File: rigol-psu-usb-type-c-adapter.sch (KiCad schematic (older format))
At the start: 12 parts

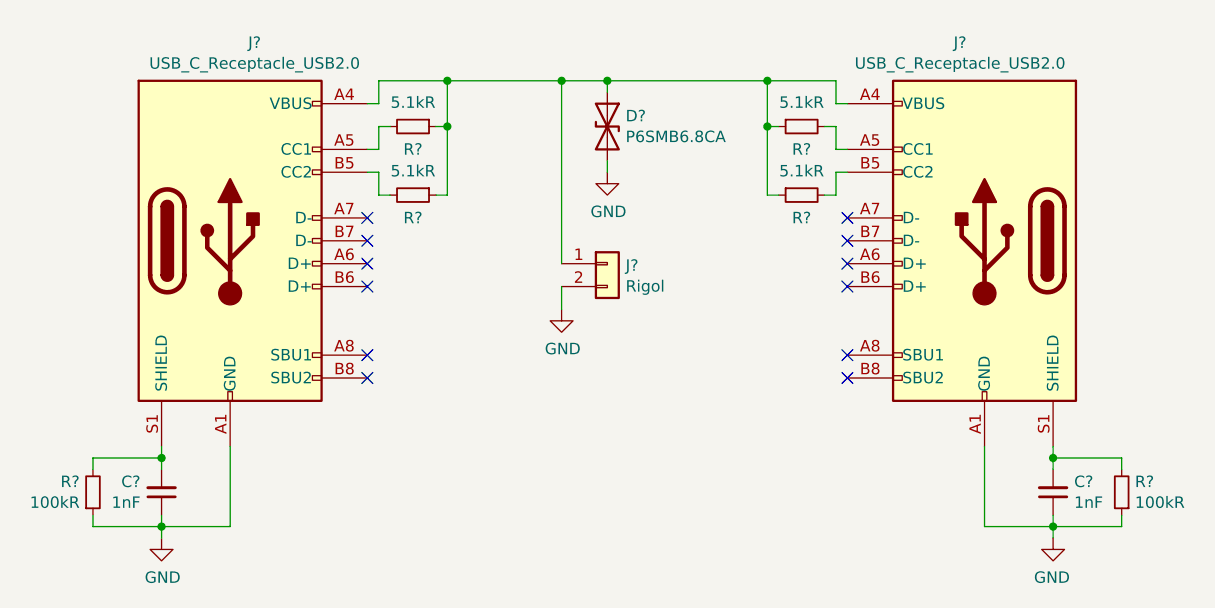
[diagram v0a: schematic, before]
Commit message: Fix CC pull-ups
Memory fooled me. They need to be 10kR, not 5.1kR.
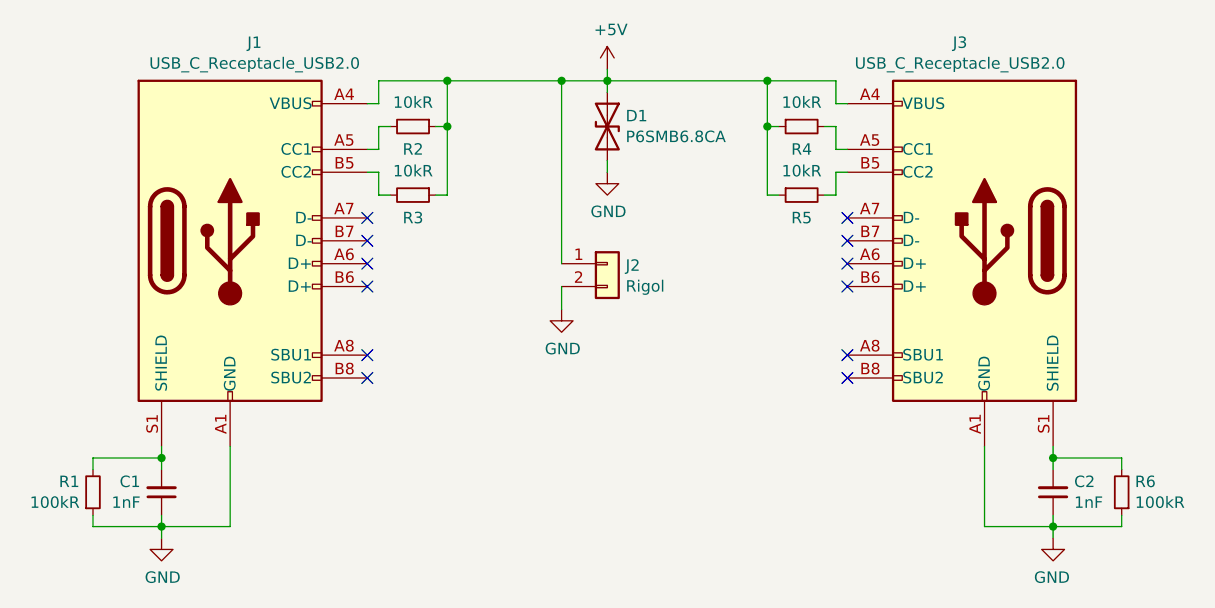
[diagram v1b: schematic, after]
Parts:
- R2, R3, R4, R5: renamed from R?; value 5.1kR -> 10kR; LCSC C25905 -> C25725
- gave numbers to parts that had none: 8
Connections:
- net +5V: now reaches D1.1 (A1), J1.A4 (VBUS), J1.A9 (VBUS), J1.B4 (VBUS), J1.B9 (VBUS), J2.1 (Pin_1), J3.A4 (VBUS), J3.A9 (VBUS), J3.B4 (VBUS), J3.B9 (VBUS), R2.1, R3.1, R4.1, R5.1
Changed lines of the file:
@@
 $EndDescr
 $Comp
-L Connector:USB_C_Receptacle_USB2.0 J?
+L Connector:USB_C_Receptacle_USB2.0 J1
 U 1 1 60DA4C0D
 P 2350 3300
-F 0 "J?" H 2457 4167 50  0000 C CNN
+F 0 "J1" H 2457 4167 50  0000 C CNN
 F 1 "USB_C_Receptacle_USB2.0" H 2457 4076 50  0000 C CNN
 F 2 "Connector_USB:USB_C_Receptacle_Palconn_UTC16-G" H 2500 3300 50  0001 C CNN
@@
 $EndComp
 $Comp
-L Device:R_Small R?
+L Device:R_Small R3
 U 1 1 60DA5B22
 P 3150 3100
-F 0 "R?" V 3250 3100 50  0000 C CNN
-F 1 "5.1kR" V 3045 3100 50  0000 C CNN
+F 0 "R3" V 3250 3100 50  0000 C CNN
+F 1 "10kR" V 3045 3100 50  0000 C CNN
 F 2 "Resistor_SMD:R_0402_1005Metric" H 3150 3100 50  0001 C CNN
 F 3 "~" H 3150 3100 50  0001 C CNN
-F 4 "C25905" H 3150 3100 50  0001 C CNN "LCSC"
+F 4 "C25725" H 3150 3100 50  0001 C CNN "LCSC"
 	1    3150 3100
 	0    1    1    0
 $EndComp
 $Comp
-L Device:R_Small R?
+L Device:R_Small R2
 U 1 1 60DA656F
 P 3150 2800
-F 0 "R?" V 3250 2800 50  0000 C CNN
-F 1 "5.1kR" V 3045 2800 50  0000 C CNN
+F 0 "R2" V 3250 2800 50  0000 C CNN
+F 1 "10kR" V 3045 2800 50  0000 C CNN
 F 2 "Resistor_SMD:R_0402_1005Metric" H 3150 2800 50  0001 C CNN
 F 3 "~" H 3150 2800 50  0001 C CNN
-F 4 "C25905" H 3150 2800 50  0001 C CNN "LCSC"
+F 4 "C25725" H 3150 2800 50  0001 C CNN "LCSC"
 	1    3150 2800
 	0    1    1    0
@@
 Connection ~ 3300 2800
 $Comp
-L Device:C_Small C?
+L Device:C_Small C1
 U 1 1 60DA87B0
 P 2050 4400
-F 0 "C?" H 1958 4354 50  0000 R CNN
+F 0 "C1" H 1958 4354 50  0000 R CNN
 F 1 "1nF" H 1958 4445 50  0000 R CNN
 F 2 "Capacitor_SMD:C_1206_3216Metric" H 2050 4400 50  0001 C CNN
@@
 $EndComp
 $Comp
-L Device:R_Small R?
+L Device:R_Small R1
 U 1 1 60DA946F
 P 1750 4400
-F 0 "R?" H 1692 4354 50  0000 R CNN
+F 0 "R1" H 1692 4354 50  0000 R CNN
 F 1 "100kR" H 1692 4445 50  0000 R CNN
 F 2 "Resistor_SMD:R_1206_3216Metric" H 1750 4400 50  0001 C CNN
@@
 	2050 4550 2050 4500
 $Comp
-L power:GND #PWR?
+L power:GND #PWR0101
 U 1 1 60DAA587
 P 2050 4600
-F 0 "#PWR?" H 2050 4350 50  0001 C CNN
+F 0 "#PWR0101" H 2050 4350 50  0001 C CNN
 F 1 "GND" H 2055 4427 50  0000 C CNN
 F 2 "" H 2050 4600 50  0001 C CNN
@@
 	2350 4200 2350 4550
 $Comp
-L Connector:USB_C_Receptacle_USB2.0 J?
+L Connector:USB_C_Receptacle_USB2.0 J3
 U 1 1 60DB2CE0
 P 5650 3300
-F 0 "J?" H 5757 4167 50  0000 C CNN
+F 0 "J3" H 5757 4167 50  0000 C CNN
 F 1 "USB_C_Receptacle_USB2.0" H 5757 4076 50  0000 C CNN
 F 2 "Connector_USB:USB_C_Receptacle_Palconn_UTC16-G" H 5800 3300 50  0001 C CNN
@@
 $EndComp
 $Comp
-L Device:R_Small R?
+L Device:R_Small R5
 U 1 1 60DB2CE7
 P 4850 3100
-F 0 "R?" V 4950 3100 50  0000 C CNN
-F 1 "5.1kR" V 4745 3100 50  0000 C CNN
+F 0 "R5" V 4950 3100 50  0000 C CNN
+F 1 "10kR" V 4745 3100 50  0000 C CNN
 F 2 "Resistor_SMD:R_0402_1005Metric" H 4850 3100 50  0001 C CNN
 F 3 "~" H 4850 3100 50  0001 C CNN
-F 4 "C25905" H 4850 3100 50  0001 C CNN "LCSC"
+F 4 "C25725" H 4850 3100 50  0001 C CNN "LCSC"
 	1    4850 3100
 	0    -1   1    0
 $EndComp
 $Comp
-L Device:R_Small R?
+L Device:R_Small R4
 U 1 1 60DB2CEE
 P 4850 2800
-F 0 "R?" V 4950 2800 50  0000 C CNN
-F 1 "5.1kR" V 4745 2800 50  0000 C CNN
+F 0 "R4" V 4950 2800 50  0000 C CNN
+F 1 "10kR" V 4745 2800 50  0000 C CNN
 F 2 "Resistor_SMD:R_0402_1005Metric" H 4850 2800 50  0001 C CNN
 F 3 "~" H 4850 2800 50  0001 C CNN
-F 4 "C25905" H 4850 2800 50  0001 C CNN "LCSC"
+F 4 "C25725" H 4850 2800 50  0001 C CNN "LCSC"
 	1    4850 2800
 	0    -1   1    0
@@
 Connection ~ 4700 2800
 $Comp
-L Device:C_Small C?
+L Device:C_Small C2
 U 1 1 60DB2D03
 P 5950 4400
-F 0 "C?" H 5858 4354 50  0000 R CNN
+F 0 "C2" H 5858 4354 50  0000 R CNN
 F 1 "1nF" H 5858 4445 50  0000 R CNN
 F 2 "Capacitor_SMD:C_1206_3216Metric" H 5950 4400 50  0001 C CNN
@@
 $EndComp
 $Comp
-L Device:R_Small R?
+L Device:R_Small R6
 U 1 1 60DB2D0A
 P 6250 4400
-F 0 "R?" H 6192 4354 50  0000 R CNN
+F 0 "R6" H 6192 4354 50  0000 R CNN
 F 1 "100kR" H 6192 4445 50  0000 R CNN
 F 2 "Resistor_SMD:R_1206_3216Metric" H 6250 4400 50  0001 C CNN
@@
 	5950 4550 5950 4500
 $Comp
-L power:GND #PWR?
+L power:GND #PWR0102
 U 1 1 60DB2D18
 P 5950 4600
-F 0 "#PWR?" H 5950 4350 50  0001 C CNN
+F 0 "#PWR0102" H 5950 4350 50  0001 C CNN
 F 1 "GND" H 5955 4427 50  0000 C CNN
 F 2 "" H 5950 4600 50  0001 C CNN
@@
 	5650 4200 5650 4550
 $Comp
-L Device:D_TVS D?
+L Device:D_TVS D1
 U 1 1 60DB3868
 P 4000 2800
-F 0 "D?" V 3954 2880 50  0000 L CNN
+F 0 "D1" V 3954 2880 50  0000 L CNN
 F 1 "P6SMB6.8CA" V 4045 2880 50  0000 L CNN
 F 2 "Diode_SMD:D_SMB" H 4000 2800 50  0001 C CNN
@@
 	4000 2650 4000 2600
 $Comp
-L power:GND #PWR?
+L power:GND #PWR0103
 U 1 1 60DB5B2D
 P 4000 3000
-F 0 "#PWR?" H 4000 2750 50  0001 C CNN
+F 0 "#PWR0103" H 4000 2750 50  0001 C CNN
 F 1 "GND" H 4005 2827 50  0000 C CNN
 F 2 "" H 4000 3000 50  0001 C CNN
@@
 Connection ~ 4000 2600
 $Comp
-L Connector_Generic:Conn_01x02 J?
+L Connector_Generic:Conn_01x02 J2
 U 1 1 60DB9EB8
 P 4000 3400
-F 0 "J?" H 4080 3392 50  0000 L CNN
+F 0 "J2" H 4080 3392 50  0000 L CNN
 F 1 "Rigol" H 4080 3301 50  0000 L CNN
 F 2 "rigol-psu:DP832" H 4000 3400 50  0001 C CNN
@@
 	3800 2600 4000 2600
 $Comp
-L power:GND #PWR?
+L power:GND #PWR0104
 U 1 1 60DBB222
 P 3800 3600
-F 0 "#PWR?" H 3800 3350 50  0001 C CNN
+F 0 "#PWR0104" H 3800 3350 50  0001 C CNN
 F 1 "GND" H 3805 3427 50  0000 C CNN
 F 2 "" H 3800 3600 50  0001 C CNN
@@
 Wire Wire Line
 	3800 3600 3800 3500
+$Comp
+L power:+5V #PWR0105
+U 1 1 60DC6362
+P 4000 2550
+F 0 "#PWR0105" H 4000 2400 50  0001 C CNN
+F 1 "+5V" H 4015 2723 50  0000 C CNN
+F 2 "" H 4000 2550 50  0001 C CNN
+F 3 "" H 4000 2550 50  0001 C CNN
+	1    4000 2550
+	1    0    0    -1
+$EndComp
+Wire Wire Line
+	4000 2550 4000 2600
 $EndSCHEMATC

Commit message: Fix CC resistor part number
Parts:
- R2, R3, R4, R5: LCSC C25725 -> C25744
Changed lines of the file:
@@
 F 2 "Resistor_SMD:R_0402_1005Metric" H 3150 3100 50  0001 C CNN
 F 3 "~" H 3150 3100 50  0001 C CNN
-F 4 "C25725" H 3150 3100 50  0001 C CNN "LCSC"
+F 4 "C25744" H 3150 3100 50  0001 C CNN "LCSC"
 	1    3150 3100
 	0    1    1    0
@@
 F 2 "Resistor_SMD:R_0402_1005Metric" H 3150 2800 50  0001 C CNN
 F 3 "~" H 3150 2800 50  0001 C CNN
-F 4 "C25725" H 3150 2800 50  0001 C CNN "LCSC"
+F 4 "C25744" H 3150 2800 50  0001 C CNN "LCSC"
 	1    3150 2800
 	0    1    1    0
@@
 F 2 "Resistor_SMD:R_0402_1005Metric" H 4850 3100 50  0001 C CNN
 F 3 "~" H 4850 3100 50  0001 C CNN
-F 4 "C25725" H 4850 3100 50  0001 C CNN "LCSC"
+F 4 "C25744" H 4850 3100 50  0001 C CNN "LCSC"
 	1    4850 3100
 	0    -1   1    0
@@
 F 2 "Resistor_SMD:R_0402_1005Metric" H 4850 2800 50  0001 C CNN
 F 3 "~" H 4850 2800 50  0001 C CNN
-F 4 "C25725" H 4850 2800 50  0001 C CNN "LCSC"
+F 4 "C25744" H 4850 2800 50  0001 C CNN "LCSC"
 	1    4850 2800
 	0    -1   1    0
